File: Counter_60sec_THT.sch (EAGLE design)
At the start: 39 parts, among them IC1 74LS90N, IC10 7805T, IC2 74LS90N, IC3 74LS48N, IC4 74LS48N, IC5 74ALS08N, IC6 LM555N, IC7 74LS14N, IC8 7476N, IC9 74LS32N

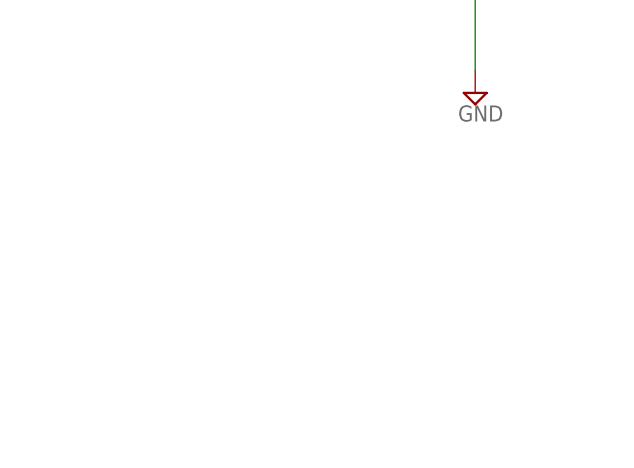
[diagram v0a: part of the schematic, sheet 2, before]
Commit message: [Zach] Added heatsink
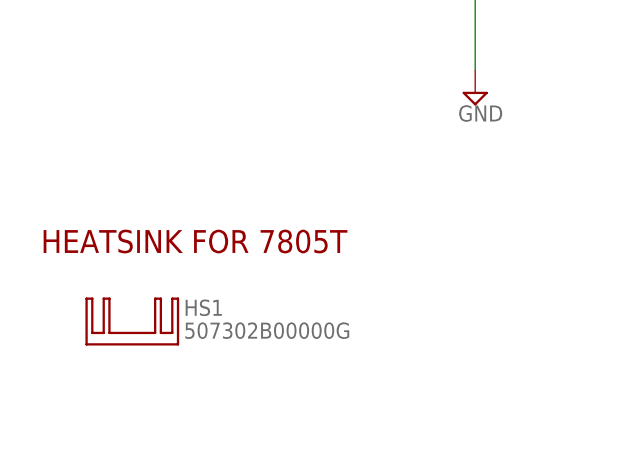
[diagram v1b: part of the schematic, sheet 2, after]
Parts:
- added HS1: 507302B00000G, to220-heatsink:507302B00000G
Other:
- note added: "HEATSINK FOR 7805T"
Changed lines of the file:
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@@
 <part name="S1" library="switch-omron" deviceset="10-XX" device="" package3d_urn="urn:adsk.eagle:package:41056974/2"/>
 <part name="S2" library="switch-omron" deviceset="10-XX" device="" package3d_urn="urn:adsk.eagle:package:41056974/2"/>
+<part name="HS1" library="to220-heatsink" deviceset="507302B00000G" device="" package3d_urn="urn:adsk.eagle:package:41058286/10"/>
 </parts>
 <sheets>
@@
 <text x="109.22" y="76.2" size="1.778" layer="94">Schmitt trigger inverter</text>
 <text x="160.02" y="83.82" size="1.778" layer="94">J-K Flip-Flop</text>
+<text x="12.7" y="27.94" size="2.54" layer="94">HEATSINK FOR 7805T</text>
 </plain>
 <instances>
@@
 <attribute name="VALUE" x="147.955" y="146.05" size="1.778" layer="96"/>
 </instance>
+<instance part="HS1" gate="G$1" x="22.86" y="17.78" smashed="yes">
+<attribute name="NAME" x="28.575" y="20.955" size="1.778" layer="95"/>
+<attribute name="VALUE" x="28.575" y="18.415" size="1.778" layer="96"/>
+</instance>
 </instances>
